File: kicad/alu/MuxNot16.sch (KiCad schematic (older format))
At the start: 16 parts, among them U19 SN74ALVC00, U20 SN74ALVC00, U21 SN74ALVC00, U22 SN74ALVC00, U23 SN74ALVC00, U24 SN74ALVC00, U25 SN74ALVC00, U26 SN74ALVC00, U27 SN74ALVC00, U28 SN74ALVC00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

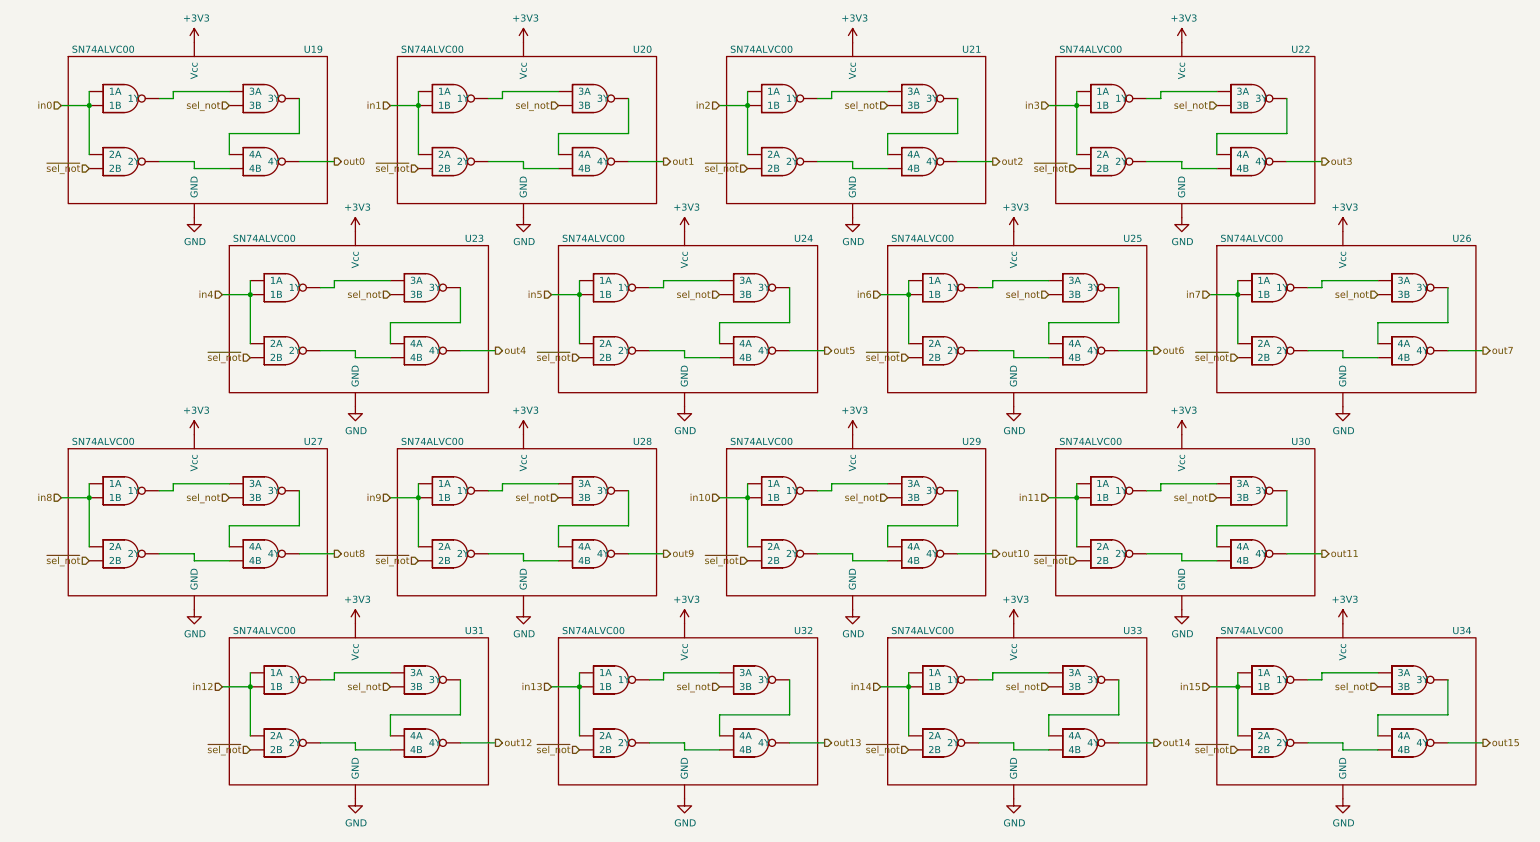
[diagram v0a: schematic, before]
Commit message: ALU schematic, layout, routing complete. Associated motherboardmod. Also added Load LED to register and program counter boards.
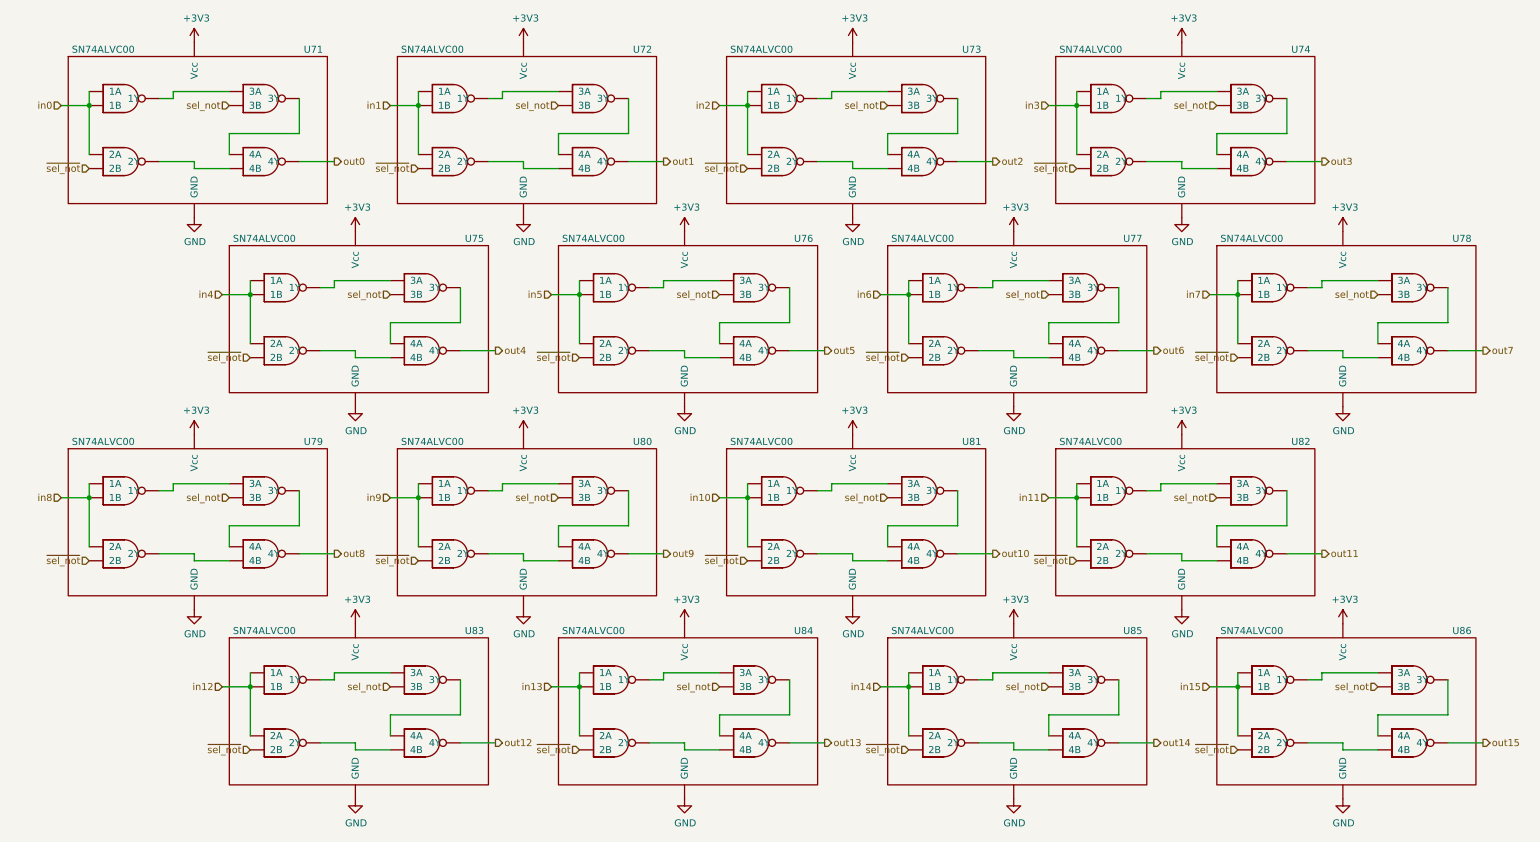
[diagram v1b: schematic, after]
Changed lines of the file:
@@
 AR Path="/5EBF23E3/5EA41C2F" Ref="U35"  Part="1"
 AR Path="/5F096D99/5EA41C2F" Ref="U71"  Part="1"
-F 0 "U19" H 2600 150 50  0000 C CNN
+F 0 "U71" H 2600 150 50  0000 C CNN
 F 1 "SN74ALVC00" H 1100 150 50  0000 C CNN
 F 2 "Package_SO:TSSOP-14_4.4x5mm_P0.65mm" H 1750 -1000 50  0001 C CNN
@@
 AR Path="/5EBF23E3/5EB42006" Ref="U36"  Part="1"
 AR Path="/5F096D99/5EB42006" Ref="U72"  Part="1"
-F 0 "U20" H 4950 150 50  0000 C CNN
+F 0 "U72" H 4950 150 50  0000 C CNN
 F 1 "SN74ALVC00" H 3450 150 50  0000 C CNN
 F 2 "Package_SO:TSSOP-14_4.4x5mm_P0.65mm" H 4100 -1000 50  0001 C CNN
@@
 AR Path="/5EBF23E3/5EB457F9" Ref="U37"  Part="1"
 AR Path="/5F096D99/5EB457F9" Ref="U73"  Part="1"
-F 0 "U21" H 7300 150 50  0000 C CNN
+F 0 "U73" H 7300 150 50  0000 C CNN
 F 1 "SN74ALVC00" H 5800 150 50  0000 C CNN
 F 2 "Package_SO:TSSOP-14_4.4x5mm_P0.65mm" H 6450 -1000 50  0001 C CNN
@@
 AR Path="/5EBF23E3/5EB4A7EC" Ref="U38"  Part="1"
 AR Path="/5F096D99/5EB4A7EC" Ref="U74"  Part="1"
-F 0 "U22" H 9650 150 50  0000 C CNN
+F 0 "U74" H 9650 150 50  0000 C CNN
 F 1 "SN74ALVC00" H 8150 150 50  0000 C CNN
 F 2 "Package_SO:TSSOP-14_4.4x5mm_P0.65mm" H 8800 -1000 50  0001 C CNN
@@
 AR Path="/5EBF23E3/5EB5C151" Ref="U39"  Part="1"
 AR Path="/5F096D99/5EB5C151" Ref="U75"  Part="1"
-F 0 "U23" H 3750 1500 50  0000 C CNN
+F 0 "U75" H 3750 1500 50  0000 C CNN
 F 1 "SN74ALVC00" H 2250 1500 50  0000 C CNN
 F 2 "Package_SO:TSSOP-14_4.4x5mm_P0.65mm" H 2900 350 50  0001 C CNN
@@
 AR Path="/5EBF23E3/5EB5C176" Ref="U40"  Part="1"
 AR Path="/5F096D99/5EB5C176" Ref="U76"  Part="1"
-F 0 "U24" H 6100 1500 50  0000 C CNN
+F 0 "U76" H 6100 1500 50  0000 C CNN
 F 1 "SN74ALVC00" H 4600 1500 50  0000 C CNN
 F 2 "Package_SO:TSSOP-14_4.4x5mm_P0.65mm" H 5250 350 50  0001 C CNN
@@
 AR Path="/5EBF23E3/5EB5C19B" Ref="U41"  Part="1"
 AR Path="/5F096D99/5EB5C19B" Ref="U77"  Part="1"
-F 0 "U25" H 8450 1500 50  0000 C CNN
+F 0 "U77" H 8450 1500 50  0000 C CNN
 F 1 "SN74ALVC00" H 6950 1500 50  0000 C CNN
 F 2 "Package_SO:TSSOP-14_4.4x5mm_P0.65mm" H 7600 350 50  0001 C CNN
@@
 AR Path="/5EBF23E3/5EB5C1C0" Ref="U42"  Part="1"
 AR Path="/5F096D99/5EB5C1C0" Ref="U78"  Part="1"
-F 0 "U26" H 10800 1500 50  0000 C CNN
+F 0 "U78" H 10800 1500 50  0000 C CNN
 F 1 "SN74ALVC00" H 9300 1500 50  0000 C CNN
 F 2 "Package_SO:TSSOP-14_4.4x5mm_P0.65mm" H 9950 350 50  0001 C CNN
@@
 AR Path="/5EBF23E3/5EB78A9D" Ref="U43"  Part="1"
 AR Path="/5F096D99/5EB78A9D" Ref="U79"  Part="1"
-F 0 "U27" H 2600 2950 50  0000 C CNN
+F 0 "U79" H 2600 2950 50  0000 C CNN
 F 1 "SN74ALVC00" H 1100 2950 50  0000 C CNN
 F 2 "Package_SO:TSSOP-14_4.4x5mm_P0.65mm" H 1750 1800 50  0001 C CNN
@@
 AR Path="/5EBF23E3/5EB78AC2" Ref="U44"  Part="1"
 AR Path="/5F096D99/5EB78AC2" Ref="U80"  Part="1"
-F 0 "U28" H 4950 2950 50  0000 C CNN
+F 0 "U80" H 4950 2950 50  0000 C CNN
 F 1 "SN74ALVC00" H 3450 2950 50  0000 C CNN
 F 2 "Package_SO:TSSOP-14_4.4x5mm_P0.65mm" H 4100 1800 50  0001 C CNN
@@
 AR Path="/5EBF23E3/5EB78AE7" Ref="U45"  Part="1"
 AR Path="/5F096D99/5EB78AE7" Ref="U81"  Part="1"
-F 0 "U29" H 7300 2950 50  0000 C CNN
+F 0 "U81" H 7300 2950 50  0000 C CNN
 F 1 "SN74ALVC00" H 5800 2950 50  0000 C CNN
 F 2 "Package_SO:TSSOP-14_4.4x5mm_P0.65mm" H 6450 1800 50  0001 C CNN
@@
 AR Path="/5EBF23E3/5EB78B0C" Ref="U46"  Part="1"
 AR Path="/5F096D99/5EB78B0C" Ref="U82"  Part="1"
-F 0 "U30" H 9650 2950 50  0000 C CNN
+F 0 "U82" H 9650 2950 50  0000 C CNN
 F 1 "SN74ALVC00" H 8150 2950 50  0000 C CNN
 F 2 "Package_SO:TSSOP-14_4.4x5mm_P0.65mm" H 8800 1800 50  0001 C CNN
@@
 AR Path="/5EBF23E3/5EB78B31" Ref="U47"  Part="1"
 AR Path="/5F096D99/5EB78B31" Ref="U83"  Part="1"
-F 0 "U31" H 3750 4300 50  0000 C CNN
+F 0 "U83" H 3750 4300 50  0000 C CNN
 F 1 "SN74ALVC00" H 2250 4300 50  0000 C CNN
 F 2 "Package_SO:TSSOP-14_4.4x5mm_P0.65mm" H 2900 3150 50  0001 C CNN
@@
 AR Path="/5EBF23E3/5EB78B56" Ref="U48"  Part="1"
 AR Path="/5F096D99/5EB78B56" Ref="U84"  Part="1"
-F 0 "U32" H 6100 4300 50  0000 C CNN
+F 0 "U84" H 6100 4300 50  0000 C CNN
 F 1 "SN74ALVC00" H 4600 4300 50  0000 C CNN
 F 2 "Package_SO:TSSOP-14_4.4x5mm_P0.65mm" H 5250 3150 50  0001 C CNN
@@
 AR Path="/5EBF23E3/5EB78B7B" Ref="U49"  Part="1"
 AR Path="/5F096D99/5EB78B7B" Ref="U85"  Part="1"
-F 0 "U33" H 8450 4300 50  0000 C CNN
+F 0 "U85" H 8450 4300 50  0000 C CNN
 F 1 "SN74ALVC00" H 6950 4300 50  0000 C CNN
 F 2 "Package_SO:TSSOP-14_4.4x5mm_P0.65mm" H 7600 3150 50  0001 C CNN
@@
 AR Path="/5EBF23E3/5EB78BA0" Ref="U50"  Part="1"
 AR Path="/5F096D99/5EB78BA0" Ref="U86"  Part="1"
-F 0 "U34" H 10800 4300 50  0000 C CNN
+F 0 "U86" H 10800 4300 50  0000 C CNN
 F 1 "SN74ALVC00" H 9300 4300 50  0000 C CNN
 F 2 "Package_SO:TSSOP-14_4.4x5mm_P0.65mm" H 9950 3150 50  0001 C CNN
